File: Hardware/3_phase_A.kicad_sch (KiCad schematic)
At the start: 17 parts

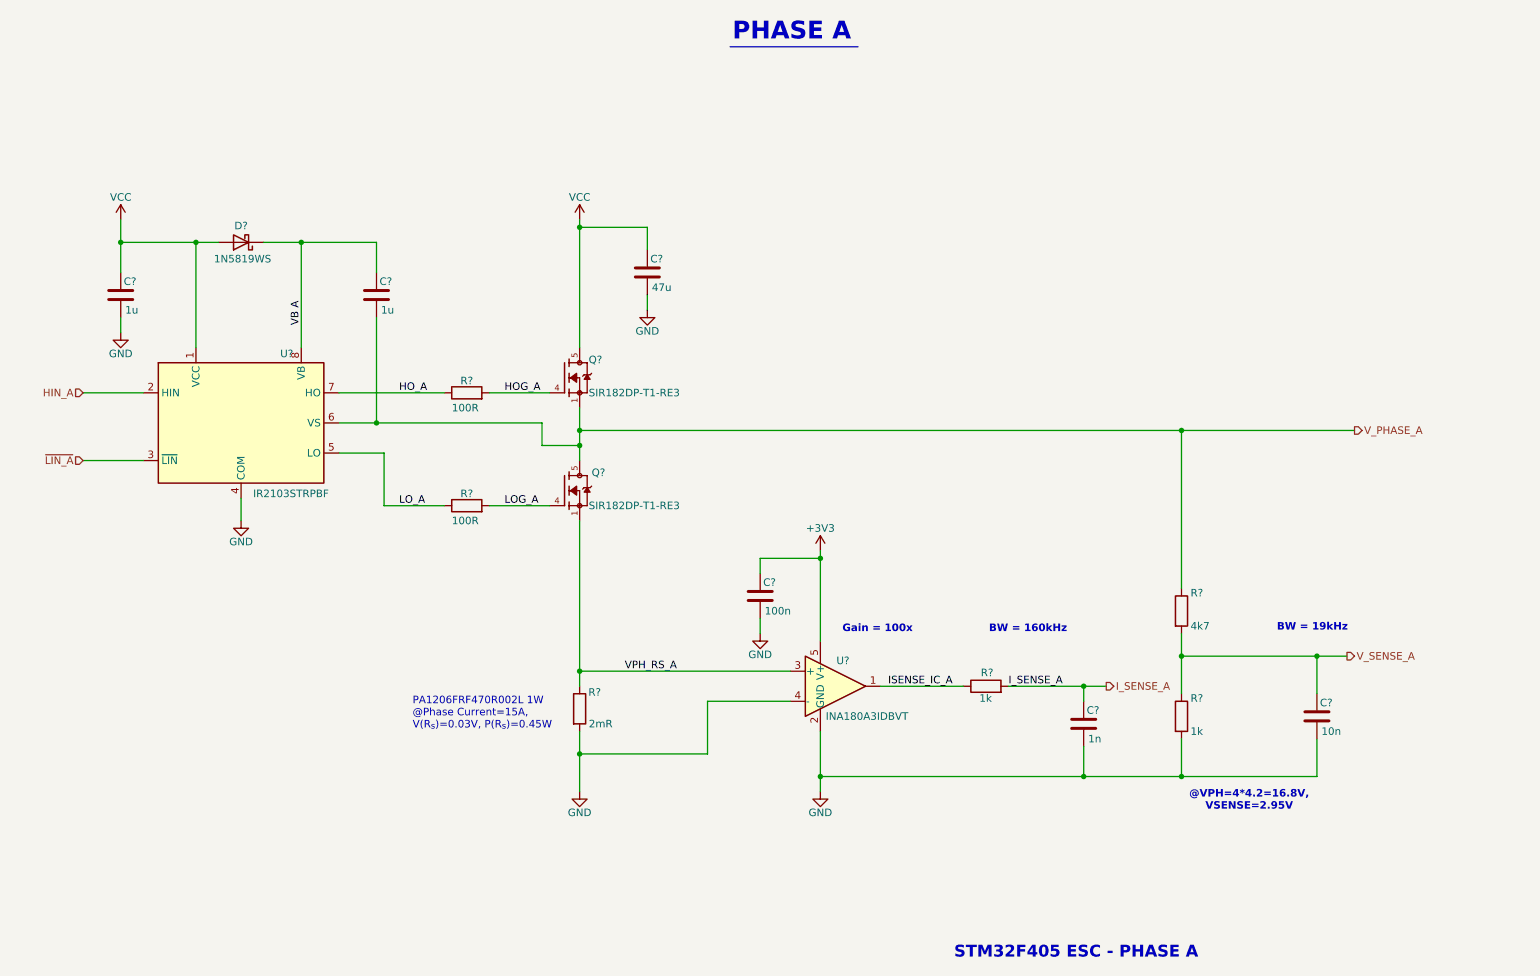
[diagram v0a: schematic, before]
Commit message: feat: Update to use I2C stemma connector
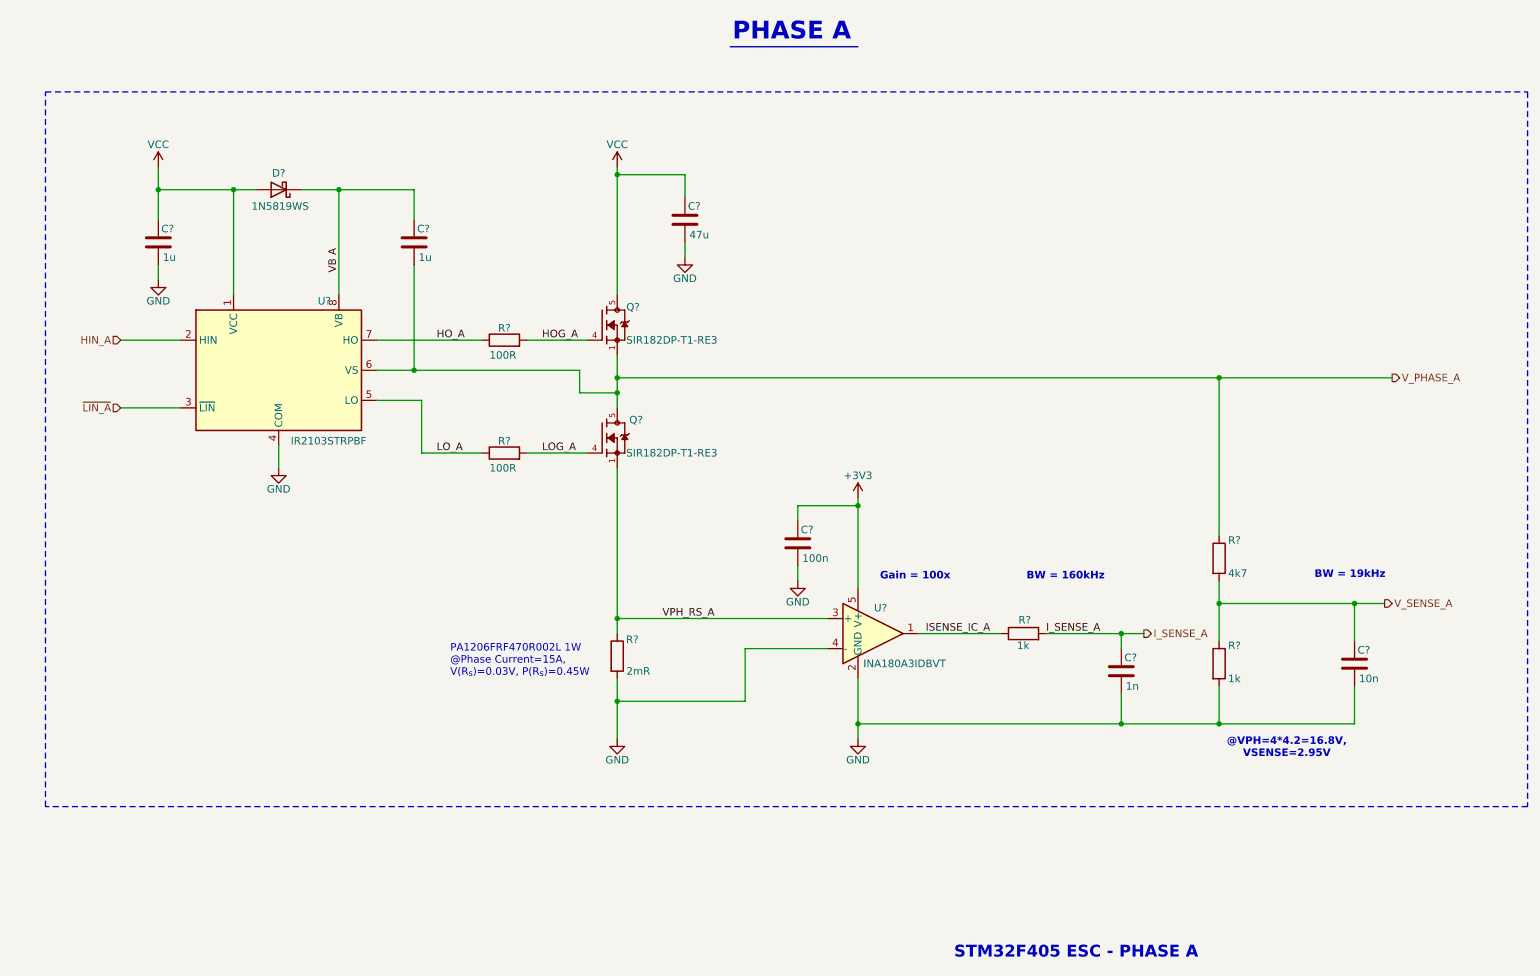
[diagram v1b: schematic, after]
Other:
- moved on the sheet: C?, D?, Q?, R?, U?
